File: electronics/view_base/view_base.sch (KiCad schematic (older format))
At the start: 92 parts, among them J1 BLDC, J2 USB_C_Receptacle_USB2.0, J3 LCD, J4 Strain, J5 Strain, Q1 MMBT4403, Q2 UMH3N, U1 MT6701-CT, U2 T-Micro32_Plus, U3 CH340C, U4 HX711, U5 TMC6300, U6 AP1117-33, U7 SN74LV1T34DBV, U8 VEML7700

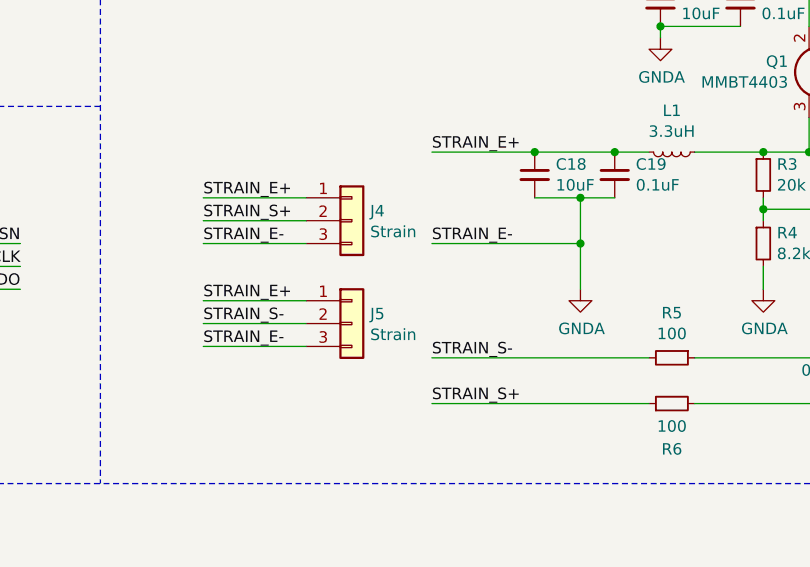
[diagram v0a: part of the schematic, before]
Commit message: View: improve silk
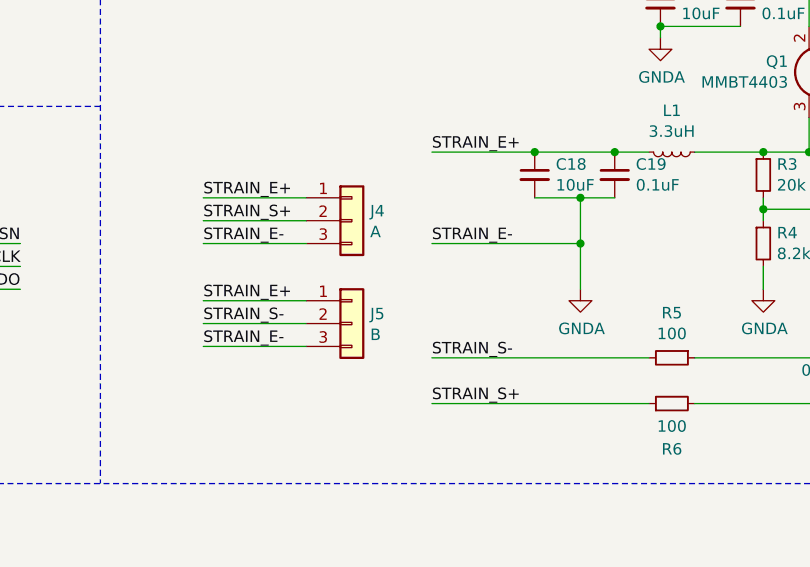
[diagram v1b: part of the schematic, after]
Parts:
- J4: value Strain -> A; footprint SolderPads:SolderPads_2mm_3 -> SolderPads:SolderPads_2mm_3_STRAIN
- J5: value Strain -> B; footprint SolderPads:SolderPads_2mm_3 -> SolderPads:SolderPads_2mm_3_STRAIN
- TP1, TP10, TP11, TP12, TP2, TP3, TP4, TP5, TP6, TP7, TP8, TP9: footprint TestPoint:TestPoint_Pad_D2.0mm -> Modified:TestPoint_Pad_D2.0mm_ValueSilk
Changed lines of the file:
@@
 P 5450 7450
 F 0 "J4" H 5530 7492 50  0000 L CNN
-F 1 "Strain" H 5530 7401 50  0000 L CNN
-F 2 "SolderPads:SolderPads_2mm_3" H 5450 7450 50  0001 C CNN
+F 1 "A" H 5530 7401 50  0000 L CNN
+F 2 "SolderPads:SolderPads_2mm_3_STRAIN" H 5450 7450 50  0001 C CNN
 F 3 "~" H 5450 7450 50  0001 C CNN
 	1    5450 7450
@@
 P 5450 7900
 F 0 "J5" H 5530 7942 50  0000 L CNN
-F 1 "Strain" H 5530 7851 50  0000 L CNN
-F 2 "SolderPads:SolderPads_2mm_3" H 5450 7900 50  0001 C CNN
+F 1 "B" H 5530 7851 50  0000 L CNN
+F 2 "SolderPads:SolderPads_2mm_3_STRAIN" H 5450 7900 50  0001 C CNN
 F 3 "~" H 5450 7900 50  0001 C CNN
 	1    5450 7900
@@
 F 0 "TP1" H 1098 1096 50  0000 L CNN
 F 1 "5V" H 1098 1005 50  0000 L CNN
-F 2 "TestPoint:TestPoint_Pad_D2.0mm" H 1250 1050 50  0001 C CNN
+F 2 "Modified:TestPoint_Pad_D2.0mm_ValueSilk" H 1250 1050 50  0001 C CNN
 F 3 "~" H 1250 1050 50  0001 C CNN
 	1    1050 1050
@@
 F 0 "TP2" H 2798 1096 50  0000 L CNN
 F 1 "3.3v" H 2798 1005 50  0000 L CNN
-F 2 "TestPoint:TestPoint_Pad_D2.0mm" H 2950 1050 50  0001 C CNN
+F 2 "Modified:TestPoint_Pad_D2.0mm_ValueSilk" H 2950 1050 50  0001 C CNN
 F 3 "~" H 2950 1050 50  0001 C CNN
 	1    2750 1050
@@
 F 0 "TP3" H 2048 1646 50  0000 L CNN
 F 1 "GND" H 2048 1555 50  0000 L CNN
-F 2 "TestPoint:TestPoint_Pad_D2.0mm" H 2200 1600 50  0001 C CNN
+F 2 "Modified:TestPoint_Pad_D2.0mm_ValueSilk" H 2200 1600 50  0001 C CNN
 F 3 "~" H 2200 1600 50  0001 C CNN
 	1    2000 1600
@@
 F 0 "TP12" H 2298 9296 50  0000 L CNN
 F 1 "LED" H 2298 9205 50  0000 L CNN
-F 2 "TestPoint:TestPoint_Pad_D2.0mm" H 2450 9250 50  0001 C CNN
+F 2 "Modified:TestPoint_Pad_D2.0mm_ValueSilk" H 2450 9250 50  0001 C CNN
 F 3 "~" H 2450 9250 50  0001 C CNN
 	1    2250 9250
@@
 F 0 "TP9" H 3248 7646 50  0000 L CNN
 F 1 "CSN" H 3250 7600 50  0000 L CNN
-F 2 "TestPoint:TestPoint_Pad_D2.0mm" H 3400 7600 50  0001 C CNN
+F 2 "Modified:TestPoint_Pad_D2.0mm_ValueSilk" H 3400 7600 50  0001 C CNN
 F 3 "~" H 3400 7600 50  0001 C CNN
 	1    3200 7600
@@
 F 0 "TP10" H 3248 7746 50  0000 L CNN
 F 1 "CLK" H 3250 7700 50  0000 L CNN
-F 2 "TestPoint:TestPoint_Pad_D2.0mm" H 3400 7700 50  0001 C CNN
+F 2 "Modified:TestPoint_Pad_D2.0mm_ValueSilk" H 3400 7700 50  0001 C CNN
 F 3 "~" H 3400 7700 50  0001 C CNN
 	1    3200 7700
@@
 F 0 "TP11" H 3248 7846 50  0000 L CNN
 F 1 "DO" H 3250 7800 50  0000 L CNN
-F 2 "TestPoint:TestPoint_Pad_D2.0mm" H 3400 7800 50  0001 C CNN
+F 2 "Modified:TestPoint_Pad_D2.0mm_ValueSilk" H 3400 7800 50  0001 C CNN
 F 3 "~" H 3400 7800 50  0001 C CNN
 	1    3200 7800
@@
 F 0 "TP6" H 14998 6646 50  0000 L CNN
 F 1 "U" H 15000 6600 50  0000 L CNN
-F 2 "TestPoint:TestPoint_Pad_D2.0mm" H 15150 6600 50  0001 C CNN
+F 2 "Modified:TestPoint_Pad_D2.0mm_ValueSilk" H 15150 6600 50  0001 C CNN
 F 3 "~" H 15150 6600 50  0001 C CNN
 	1    14950 6600
@@
 F 0 "TP7" H 14998 6746 50  0000 L CNN
 F 1 "V" H 15000 6700 50  0000 L CNN
-F 2 "TestPoint:TestPoint_Pad_D2.0mm" H 15150 6700 50  0001 C CNN
+F 2 "Modified:TestPoint_Pad_D2.0mm_ValueSilk" H 15150 6700 50  0001 C CNN
 F 3 "~" H 15150 6700 50  0001 C CNN
 	1    14950 6700
@@
 F 0 "TP8" H 14998 6846 50  0000 L CNN
 F 1 "W" H 15000 6800 50  0000 L CNN
-F 2 "TestPoint:TestPoint_Pad_D2.0mm" H 15150 6800 50  0001 C CNN
+F 2 "Modified:TestPoint_Pad_D2.0mm_ValueSilk" H 15150 6800 50  0001 C CNN
 F 3 "~" H 15150 6800 50  0001 C CNN
 	1    14950 6800
@@
 F 0 "TP4" H 6598 5346 50  0000 L CNN
 F 1 "SDA" H 6600 5300 50  0000 L CNN
-F 2 "TestPoint:TestPoint_Pad_D2.0mm" H 6750 5300 50  0001 C CNN
+F 2 "Modified:TestPoint_Pad_D2.0mm_ValueSilk" H 6750 5300 50  0001 C CNN
 F 3 "~" H 6750 5300 50  0001 C CNN
 	1    6550 5300
@@
 F 0 "TP5" H 6598 5596 50  0000 L CNN
 F 1 "SCL" H 6600 5550 50  0000 L CNN
-F 2 "TestPoint:TestPoint_Pad_D2.0mm" H 6750 5550 50  0001 C CNN
+F 2 "Modified:TestPoint_Pad_D2.0mm_ValueSilk" H 6750 5550 50  0001 C CNN
 F 3 "~" H 6750 5550 50  0001 C CNN
 	1    6550 5550
